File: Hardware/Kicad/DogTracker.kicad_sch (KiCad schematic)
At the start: 20 parts

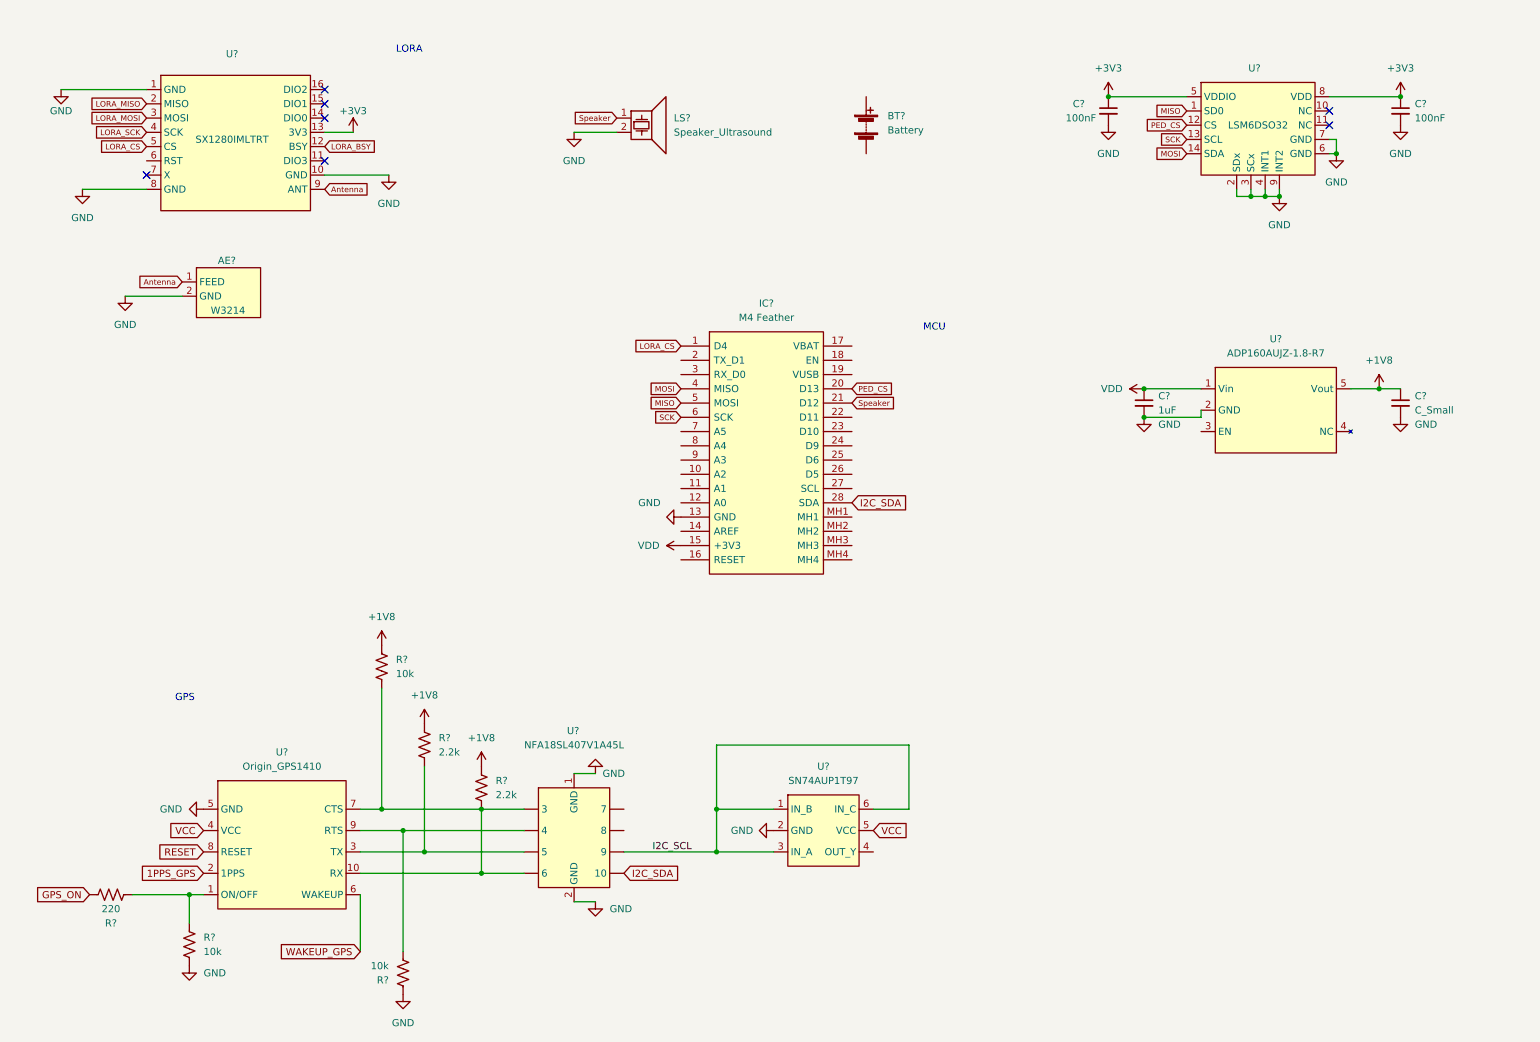
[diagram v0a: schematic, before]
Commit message: update schematic
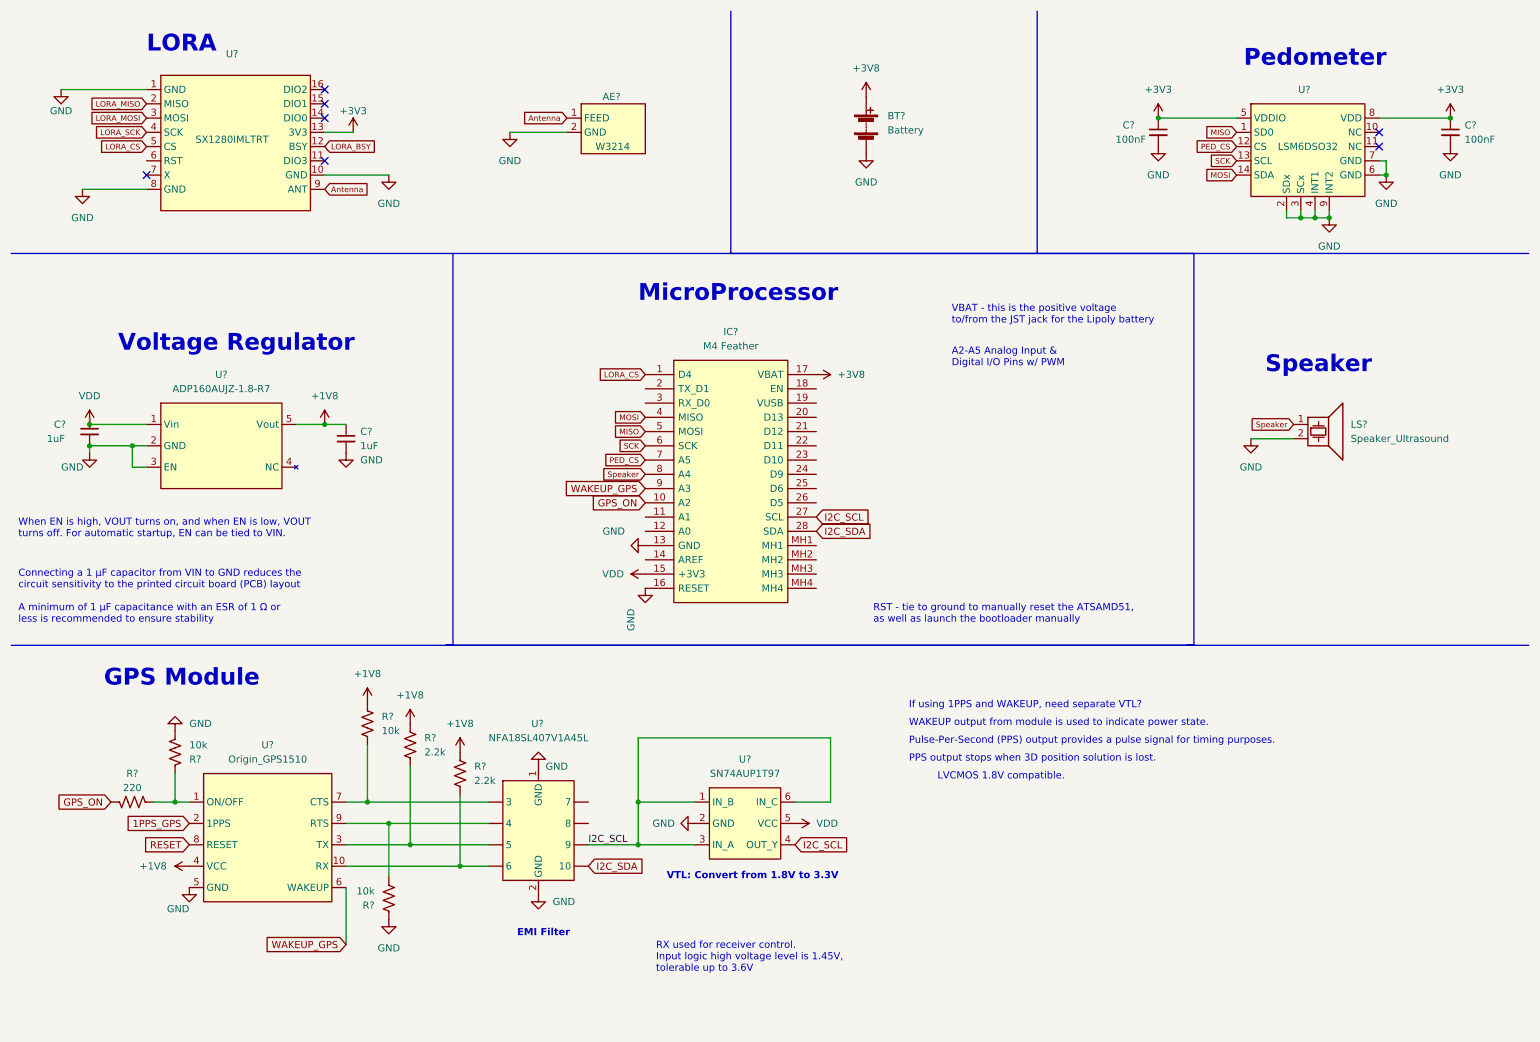
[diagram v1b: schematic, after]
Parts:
- C?: value C_Small -> 1uF
- U?: value Origin_GPS1410 -> Origin_GPS1510; symbol DogTracker:Origin_GPS1410 -> DogTracker:Origin_GPS1510
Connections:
- net +1V8: now also U?.4 (VCC)
- net GND: now also BT?.2 (-), IC?.16 (RESET), U?.3 (EN)
- net GPS_ON: now also IC?.10 (A2)
- net I2C_SCL: now also IC?.27 (SCL), U?.4 (OUT_Y)
- net PED_CS: now also IC?.7 (A5); no longer IC?.20 (D13)
- net Speaker: now also IC?.8 (A4); no longer IC?.21 (D12)
- net VDD: now also U?.5 (VCC)
- net WAKEUP_GPS: now also IC?.9 (A3)
- net +3V8: now reaches BT?.1 (+)
- net +3V8: now also IC?.17 (VBAT)
- removed net VCC: U?.4 (VCC), U?.5 (VCC)
- new net: R?.1, U?. (9), U?.10 (RX)
- new net: R?.1, U?. (9), U?.7 (CTS)
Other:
- note added: "A2-A5 Analog Input & Digital I/O Pins w/ PWM"
- note added: "Connecting a 1 μF capacitor from VIN to GND reduces the circuit sensitivity to the printed circuit board (PCB) layout A minimum of 1 μF capacitance with an ESR of 1 Ω or less is recommended to ensure stability"
- note added: "EMI Filter"
- note added: "GPS Module"
- note added: "If using 1PPS and WAKEUP, need separate VTL?"
- note added: "LVCMOS 1.8V compatible."
- note added: "MicroProcessor"
- note added: "PPS output stops when 3D position solution is lost."
- note added: "Pedometer"
- note added: "Pulse-Per-Second (PPS) output provides a pulse signal for timing purposes."
- note added: "RST - tie to ground to manually reset the ATSAMD51, as well as launch the bootloader manually"
- note added: "RX used for receiver control. Input logic high voltage level is 1.45V, tolerable up to 3.6V"
- note added: "Speaker"
- note added: "VBAT - this is the positive voltage to/from the JST jack for the Lipoly battery"
- note added: "VTL: Convert from 1.8V to 3.3V"
- note added: "Voltage Regulator"
- note added: "WAKEUP output from module is used to indicate power state."
- note added: "When EN is high, VOUT turns on, and when EN is low, VOUT turns off. For automatic startup, EN can be tied to VIN."
- note removed: "GPS"
- note removed: "MCU"
- moved on the sheet: AE?, C?, IC?, LS?, R?, U?

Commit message: update reset
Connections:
- net RESET is gone; now on net ~{RESET}: U?.8 (RESET)
- net ~{RESET}: now reaches IC?.20 (D13)
- no-connect marks 7 -> 9
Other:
- note added: "#4 - GPIO #4, PWM out #5 - GPIO #5, PWM out #6 - GPIO #6, PWM out #9 - GPIO #9, PWM out #10 - GPIO #10, PWM out #11 - GPIO #11, PWM out #12 - GPIO #12, PWM out"
- note added: "Global reset?"
- note added: "Pulse Larsen Antenna 902-928MHz"
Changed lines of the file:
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@@
   (junction (at 245.11 49.53) (diameter 0) (color 0 0 0 0)
   )
+  (no_connect (at 115.57 153.67))
   (no_connect (at 256.54 34.29))
   (no_connect (at 256.54 36.83))
@@
   (no_connect (at 68.58 31.75))
   (no_connect (at 36.83 41.91))
+  (no_connect (at 115.57 157.48))
   (wire (pts (xy 245.11 49.53) (xy 247.65 49.53))
     (stroke (width 0) (type default) (color 0 0 0 0))
@@
   (wire (pts (xy 256.54 41.91) (xy 257.81 41.91))
     (stroke (width 0) (type default) (color 0 0 0 0))
+  )
+  (text "#4 - GPIO #4, PWM out\n#5 - GPIO #5, PWM out\n#6 - GPIO #6, PWM out\n#9 - GPIO #9, PWM out\n#10 - GPIO #10, PWM out\n#11 - GPIO #11, PWM out\n#12 - GPIO #12, PWM out"
+    (at 180.34 97.79 0)
+    (effects (font (size 1.27 1.27)) (justify left bottom))
   )
   (text "VTL: Convert from 1.8V to 3.3V" (at 129.54 167.64 0)
     (effects (font (size 1.27 1.27) (thickness 0.254) bold) (justify left bottom))
   )
+  (text "Pulse Larsen Antenna 902-928MHz " (at 102.235 24.765 0)
+    (effects (font (size 1.27 1.27)) (justify left bottom))
+  )
   (text "WAKEUP output from module is used to indicate power state."
     (at 172.72 140.335 0)
@@
   )
   (text "RX used for receiver control. \nInput logic high voltage level is 1.45V, \ntolerable up to 3.6V"
-    (at 127.635 184.15 0)
+    (at 31.75 186.055 0)
     (effects (font (size 1.27 1.27)) (justify left bottom))
   )
@@
     (effects (font (size 1.27 1.27)) (justify left bottom))
   )
+  (text "Global reset?" (at 110.49 184.15 0)
+    (effects (font (size 1.27 1.27)) (justify left bottom))
+  )
   (text "Connecting a 1 μF capacitor from VIN to GND reduces the \ncircuit sensitivity to the printed circuit board (PCB) layout\n\nA minimum of 1 μF capacitance with an ESR of 1 Ω or \nless is recommended to ensure stability "
     (at 13.97 121.92 0)
@@
   )
   (text "RST - tie to ground to manually reset the ATSAMD51,\nas well as launch the bootloader manually"
-    (at 166.37 121.92 0)
+    (at 168.91 121.92 0)
     (effects (font (size 1.27 1.27)) (justify left bottom))
   )
@@
     )
   )
-  (global_label "WAKEUP_GPS" (shape input) (at 72.39 179.07 180) (fields_autoplaced)
-    (effects (font (size 1.27 1.27)) (justify right))
-    (property "Intersheet References" "${INTERSHEET_REFS}" (id 0) (at 57.7002 179.1494 0)
-      (effects (font (size 1.27 1.27)) (justify right) hide)
+  (global_label "WAKEUP_GPS" (shape output) (at 72.39 179.07 0) (fields_autoplaced)
+    (effects (font (size 1.27 1.27)) (justify left))
+    (property "Intersheet References" "${INTERSHEET_REFS}" (id 0) (at 87.0798 179.1494 0)
+      (effects (font (size 1.27 1.27)) (justify left) hide)
     )
   )
@@
     )
   )
+  (global_label "~{RESET}" (shape output) (at 156.21 85.09 0) (fields_autoplaced)
+    (effects (font (size 1.27 1.27)) (justify left))
+    (property "Intersheet References" "${INTERSHEET_REFS}" (id 0) (at 164.3683 85.0106 0)
+      (effects (font (size 1.27 1.27)) (justify left) hide)
+    )
+  )
   (global_label "LORA_BSY" (shape input) (at 68.58 36.83 0) (fields_autoplaced)
     (effects (font (size 1 1)) (justify left))
@@
     )
   )
-  (global_label "1PPS_GPS" (shape input) (at 44.45 157.48 180) (fields_autoplaced)
+  (global_label "1PPS_GPS" (shape output) (at 44.45 157.48 180) (fields_autoplaced)
     (effects (font (size 1.27 1.27)) (justify right))
     (property "Intersheet References" "${INTERSHEET_REFS}" (id 0) (at 32.3607 157.4006 0)
@@
     )
   )
-  (global_label "RESET" (shape input) (at 44.45 161.29 180) (fields_autoplaced)
+  (global_label "~{RESET}" (shape input) (at 44.45 161.29 180) (fields_autoplaced)
     (effects (font (size 1.27 1.27)) (justify right))
     (property "Intersheet References" "${INTERSHEET_REFS}" (id 0) (at 36.2917 161.2106 0)
@@
   )
   (symbol (lib_id "power:GND") (at 80.01 174.625 0) (unit 1)
-    (in_bom yes) (on_board yes) (fields_autoplaced)
+    (in_bom yes) (on_board yes)
     (property "Reference" "#PWR?" (id 0) (at 80.01 180.975 0)
       (effects (font (size 1.27 1.27)) hide)
     )
-    (property "Value" "GND" (id 1) (at 80.01 179.705 0))
+    (property "Value" "GND" (id 1) (at 83.82 174.625 0))
     (property "Footprint" "" (id 2) (at 80.01 174.625 0)
       (effects (font (size 1.27 1.27)) hide)
@@
     (pin "2")
   )
-  (symbol (lib_id "power:GND") (at 125.73 115.57 0) (unit 1)
-    (in_bom yes) (on_board yes)
-    (property "Reference" "#PWR?" (id 0) (at 125.73 121.92 0)
-      (effects (font (size 1.27 1.27)) hide)
-    )
-    (property "Value" "GND" (id 1) (at 123.19 123.19 90)
-      (effects (font (size 1.27 1.27)) (justify left))
-    )
+  (symbol (lib_id "power:GND") (at 125.73 115.57 270) (unit 1)
+    (in_bom yes) (on_board yes)
+    (property "Reference" "#PWR?" (id 0) (at 119.38 115.57 0)
+      (effects (font (size 1.27 1.27)) hide)
+    )
+    (property "Value" "GND" (id 1) (at 118.11 115.57 90)
+      (effects (font (size 1.27 1.27)) (justify left))
+    )
